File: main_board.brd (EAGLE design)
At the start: 100 x 80 mm, 95 parts, among them IC1 MBED_MICROCONTROLLER, U1 PCA9555PW,118, U11 MC33887-HSOP, U13 MC33887-HSOP, U2 SI8460AA-B-IS1, U3 MC33887-HSOP, U6 SI8460AA-B-IS1, U7 MC33887-HSOP, U8 SI8460AA-B-IS1, U9 MC33887-HSOP, X1 BALL_SENS, X10 IMU, X2 ETH, X3 ENC1, X4 ENC2, X5 BTNS, X6 ENC3, X7 ENC4, X8 ENC5, X9 COIL

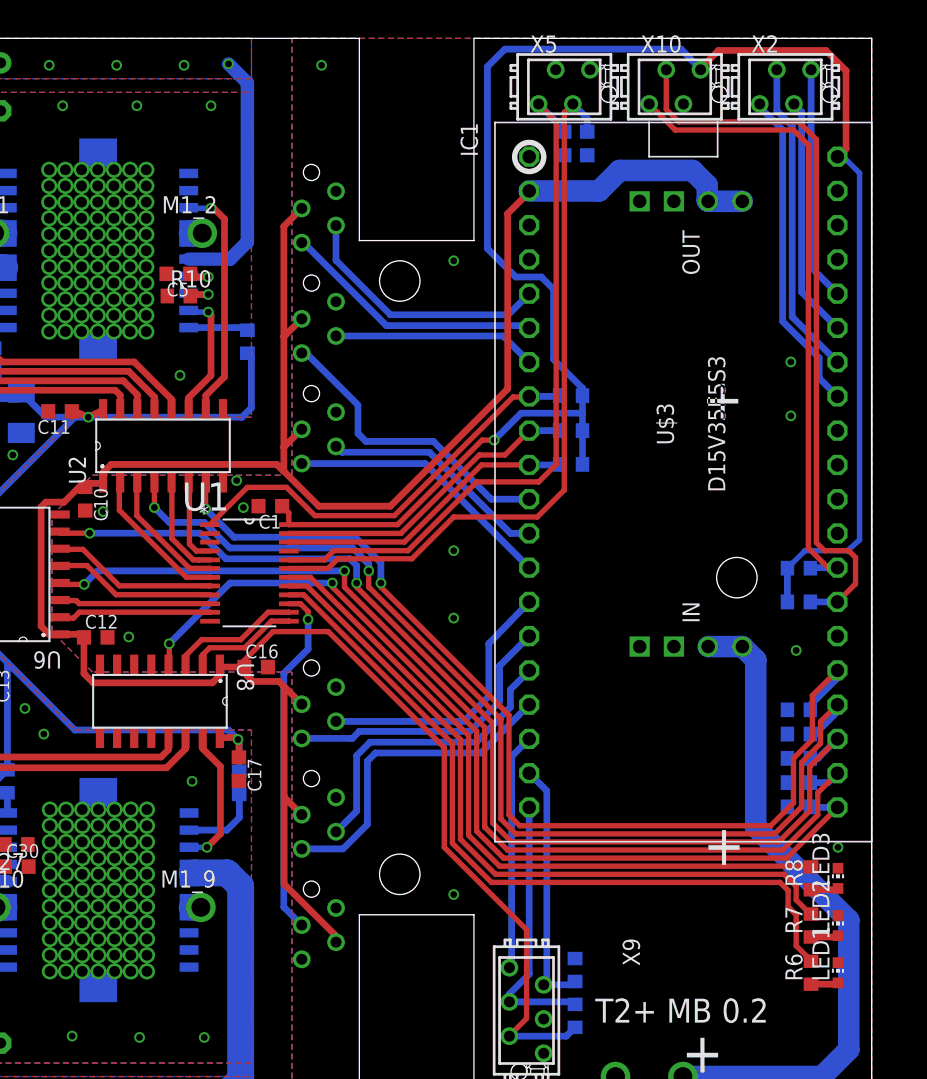
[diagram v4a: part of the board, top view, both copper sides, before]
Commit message: Added two more LEDs to IO extender pins, connected buttons directly to mbed
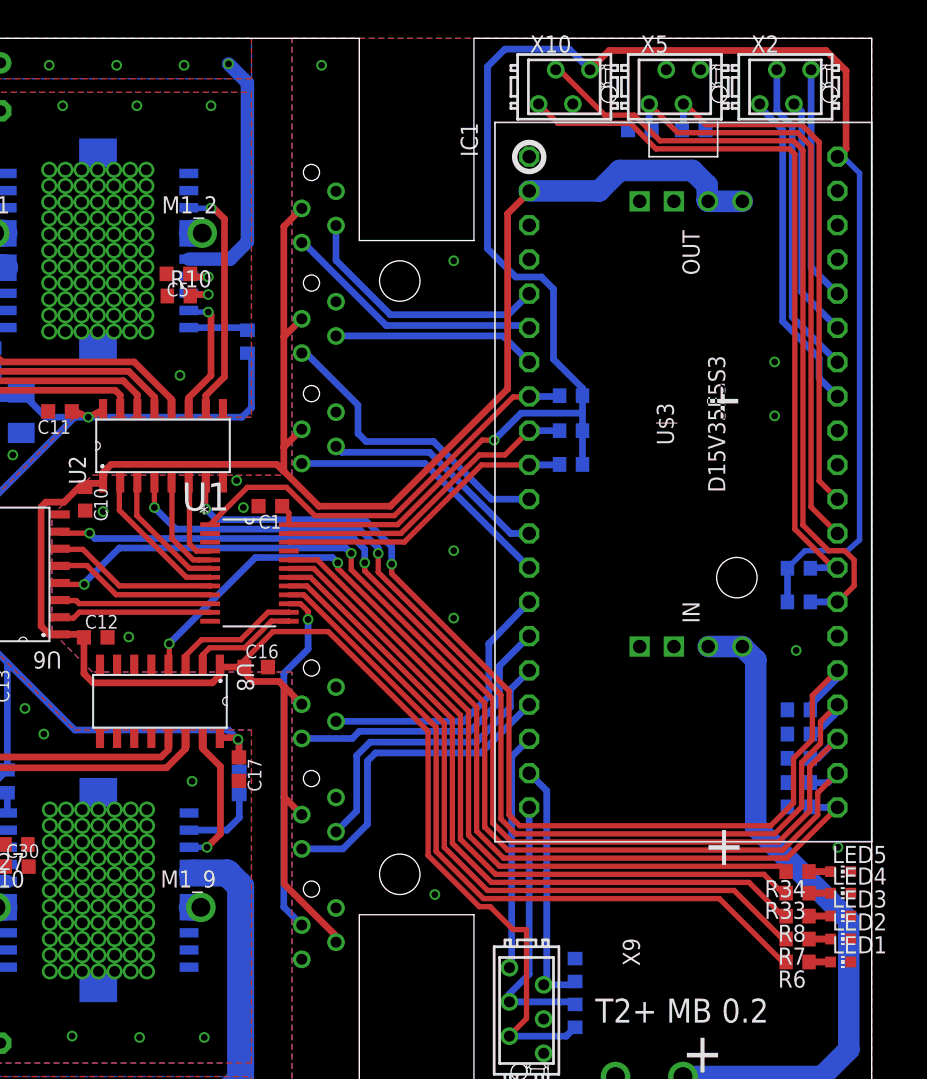
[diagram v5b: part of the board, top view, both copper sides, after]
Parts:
- added LED5, LED_5V: (no value), led:CHIP-LED0603
- added R33, R34: 2K2, rcl:R0603
- moved LED4 64.7 mm to (97.7, 16.6), flipped to the top, turned to 270 degrees
- moved X10 8.20 mm to (77.2, 76.4)
- moved X5 8.20 mm to (85.4, 76.4)
- moved C14 7.96 mm to (86.8, 73.2), turned to 180 degrees
- moved C18 5.69 mm to (82.8, 73.2), turned to 0 degrees
- moved R8 2.97 mm to (94.5, 14.9), turned to 180 degrees
- moved LED3 2.81 mm to (97.7, 14.9), turned to 270 degrees
- moved R7 1.41 mm to (94.5, 13.2), turned to 180 degrees
- moved R6 1.28 mm to (94.5, 11.5), turned to 180 degrees
- moved LED2 1.02 mm to (97.7, 13.2), turned to 270 degrees
- moved LED1 0.82 mm to (97.7, 11.5), turned to 270 degrees
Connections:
- new net LED4: R33.2, U1.19
- new net LED5: R34.2, U1.20
- new net N$11: LED4.A, R33.1
- new net N$12: LED5.A, R34.1
- net +5V: now also LED_5V.C; no longer LED4.C
- net BTN1: now also IC1.30; no longer U1.19
- net BTN2: now also IC1.29; no longer U1.20
- net GND: now also LED4.C, LED5.C
- net N$10: now also LED_5V.A; no longer LED4.A
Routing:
- net LED4: track 0.00 -> 52.2 mm
- net LED5: track 0.00 -> 51.8 mm
- net BTN1: track 54.2 -> 40.3 mm
- net BTN2: track 52.9 -> 45.0 mm
- net SDA2: track 47.8 -> 54.7 mm
- net SCL2: track 54.1 -> 59.1 mm
- net LED1: track 56.5 -> 53.5 mm
- net PWM5: track 69.6 -> 72.3 mm
- net PWM4: track 77.4 -> 79.9 mm
- net N$12: track 0.00 -> 1.60 mm
- net N$11: track 0.00 -> 1.60 mm
- net PWM1: track 76.3 -> 77.5 mm
- net PWM2: track 78.0 -> 79.1 mm
- net VCC: track 204.7 -> 205.7 mm
- net PWM3: track 80.2 -> 81.3 mm
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
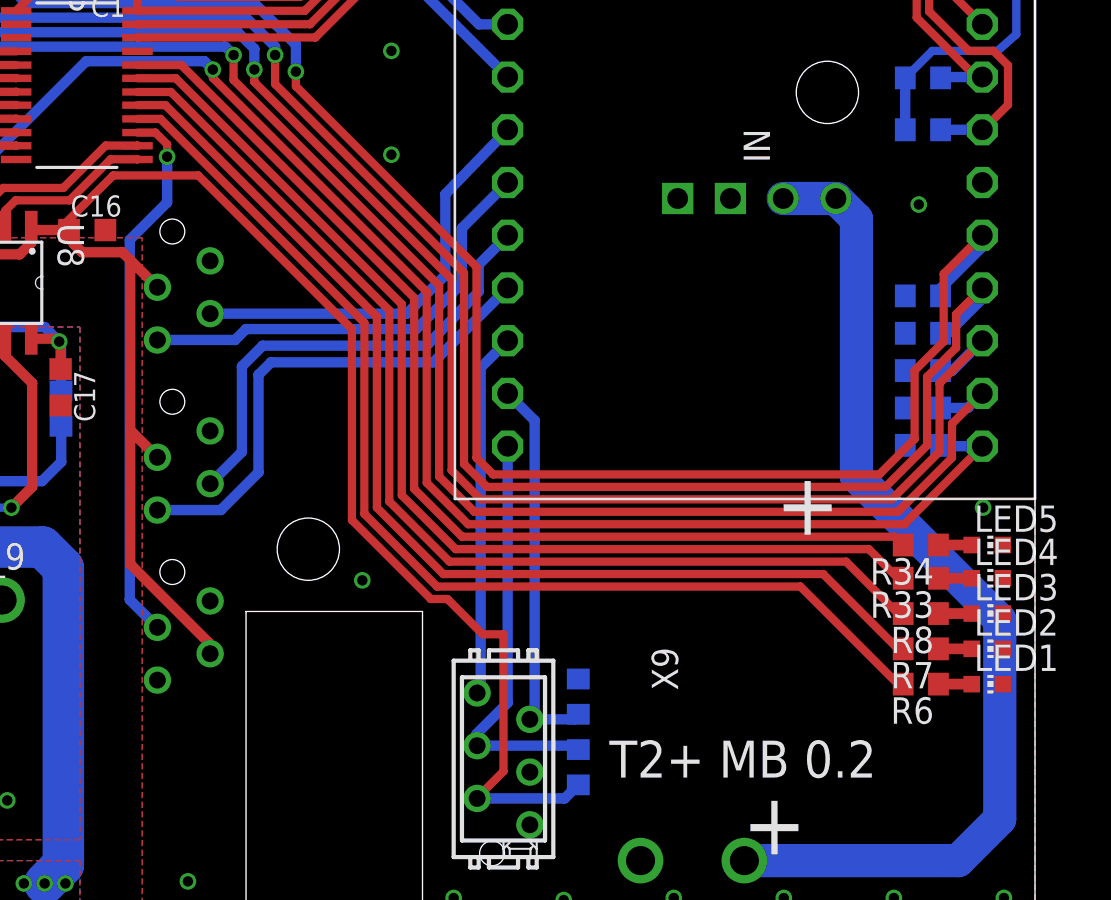
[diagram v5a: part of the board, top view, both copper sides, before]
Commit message: Connected ball detector directly to mbed
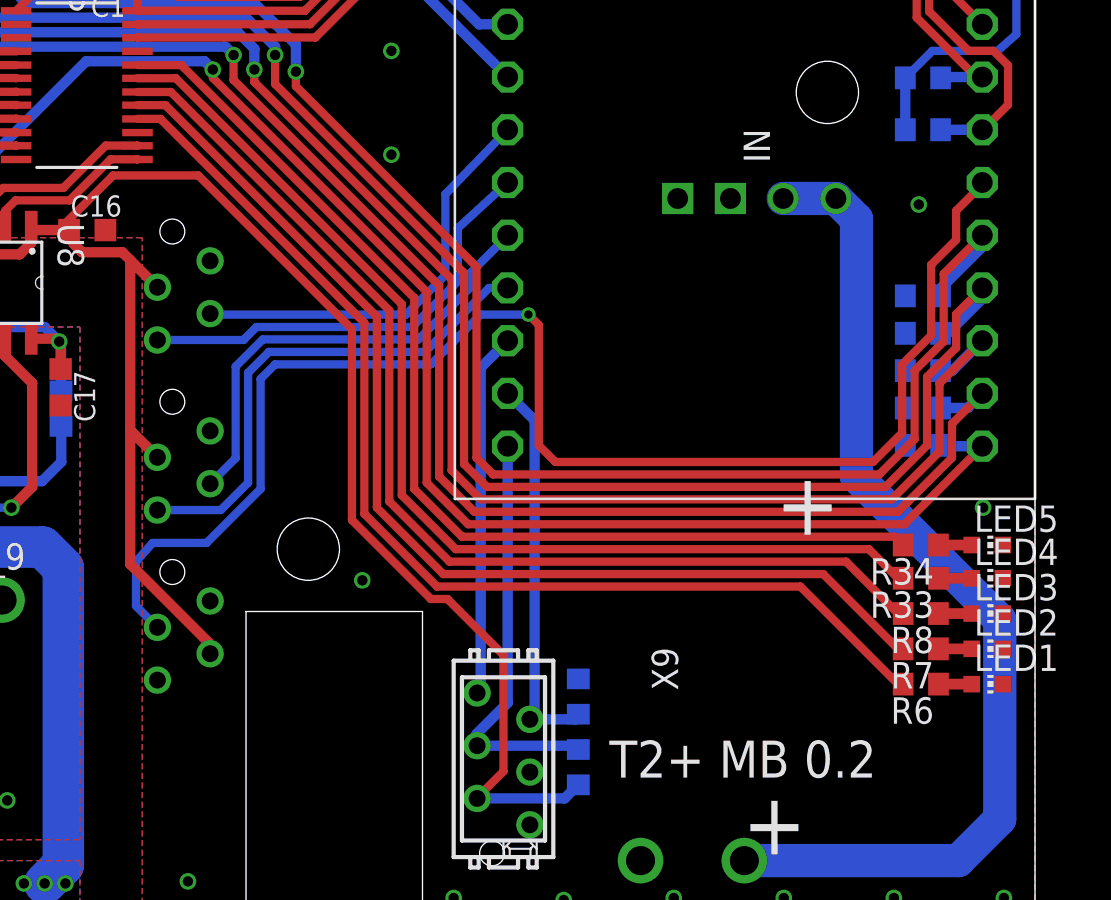
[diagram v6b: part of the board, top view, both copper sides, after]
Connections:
- net BALL: now also IC1.26; no longer U1.15
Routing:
- net BALL: track 26.2 -> 69.1 mm
- net VCC: track 205.7 -> 205.1 mm

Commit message: Few small changes
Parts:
- moved LED4 2.10 mm to (97.8, 14.5)
- moved R33 2.10 mm to (94.6, 14.5)
- moved LED1 2.10 mm to (97.8, 9.40)
- moved LED2 2.10 mm to (97.8, 11.1)
- moved LED3 2.10 mm to (97.8, 12.8)
- moved R6 2.10 mm to (94.6, 9.40)
- moved R7 2.10 mm to (94.6, 11.1)
- moved R8 2.10 mm to (94.6, 12.8)
- moved LED5 2.10 mm to (97.8, 16.1)
- moved R34 2.10 mm to (94.6, 16.1)
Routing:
- net LED1: track 53.5 -> 55.3 mm
- net LED2: track 53.1 -> 54.5 mm
- net LED5: track 51.8 -> 52.8 mm
- net LED4: track 52.2 -> 53.2 mm
- net LED3: track 52.8 -> 53.6 mm
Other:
- outline, holes or cut-outs redrawn
